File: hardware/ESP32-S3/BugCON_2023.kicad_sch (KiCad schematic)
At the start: 30 parts, among them J1 Conn_01x04_Pin, J2 Conn_01x04_Pin, J3 Conn_01x02, P1 USB_C_Plug_USB2.0, Q1 DMG3415U-7, SW1 RESET, SW2 GPIO, SW3 ON, U1 ESP32-S3-WROOM-1U-N16, U2 AP2112K-3.3

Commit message: Change Place_OLED
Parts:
- C6, C7, C8, C9: provedor (none) -> LCSC
- D1: manf# MBR120LSF -> (none)
- D2, D6, D7, D8: footprint FootprintsB:WS2812B_WDS -> FootprintsB:LED_SK6812MINI_PLCC4_3.5x3.5mm_P1.75mm
- J1: provedor (none) -> Unitelectronic
- J3: footprint Connector_PinSocket_2.54mm:PinSocket_1x02_P2.54mm_Vertical -> FootprintsB:BAT_12BH331P-GR; manf# (none) -> 12BH331P-GR
- P1: LCSC# C2760486 -> C2765186; manf# TYPE-C-31-M-31 -> (none)
- Q1: manf# DMG3415U-7 -> (none)
- R1: LCSC# C217281 -> C309083; manf# CR-03JL7---10K -> (none)
- R2, R3: LCSC# C191782 -> C204548; manf# ERJ3RBD5101V -> (none)
- R4: manf# WR06X104JTL -> (none)
- U2: LCSC# C150742 -> C51118; manf# AP7365-33WG-7 -> (none)
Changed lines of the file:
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@@
+      (effects (font (size 1.27 1.27)) hide)
+    )
+    (property "provedor" "Unitelectronic" (at 24.384 116.967 0)
       (effects (font (size 1.27 1.27)) hide)
     )
@@
       (effects (font (size 1.27 1.27)) hide)
     )
-    (property "manf#" "DMG3415U-7" (at 88.138 27.051 0)
+    (property "manf#" "" (at 88.138 27.051 0)
       (effects (font (size 1.27 1.27)) hide)
     )
@@
       (effects (font (size 1.27 1.27)) hide)
     )
+    (property "provedor" "LCSC" (at 193.294 123.444 0)
+      (effects (font (size 1.27 1.27)) hide)
+    )
     (pin "1")
     (pin "2")
@@
       (effects (font (size 1.27 1.27)))
     )
-    (property "Footprint" "FootprintsB:WS2812B_WDS" (at 236.22 143.129 0)
+    (property "Footprint" "FootprintsB:LED_SK6812MINI_PLCC4_3.5x3.5mm_P1.75mm" (at 236.22 143.129 0)
       (effects (font (size 1.27 1.27)) (justify left top) hide)
     )
@@
       (effects (font (size 1.27 1.27)) hide)
     )
-    (property "manf#" "CR-03JL7---10K" (at 103.124 107.95 0)
-      (effects (font (size 1.27 1.27)) hide)
-    )
-    (property "LCSC#" "C217281" (at 103.124 107.95 0)
+    (property "manf#" "" (at 103.124 107.95 0)
+      (effects (font (size 1.27 1.27)) hide)
+    )
+    (property "LCSC#" "C309083" (at 103.124 107.95 0)
       (effects (font (size 1.27 1.27)) hide)
     )
@@
       (effects (font (size 1.27 1.27)))
     )
-    (property "Footprint" "FootprintsB:WS2812B_WDS" (at 186.563 143.129 0)
+    (property "Footprint" "FootprintsB:LED_SK6812MINI_PLCC4_3.5x3.5mm_P1.75mm" (at 186.563 143.129 0)
       (effects (font (size 1.27 1.27)) (justify left top) hide)
     )
@@
       (effects (font (size 1.27 1.27)) hide)
     )
+    (property "provedor" "LCSC" (at 266.7 123.444 0)
+      (effects (font (size 1.27 1.27)) hide)
+    )
     (pin "1")
     (pin "2")
@@
       (effects (font (size 1.27 1.27)) hide)
     )
+    (property "provedor" "LCSC" (at 242.697 123.444 0)
+      (effects (font (size 1.27 1.27)) hide)
+    )
     (pin "1")
     (pin "2")
@@
       (effects (font (size 1.27 1.27)) hide)
     )
-    (property "manf#" "ERJ3RBD5101V" (at 46.482 26.416 0)
-      (effects (font (size 1.27 1.27)) hide)
-    )
-    (property "LCSC#" "C191782" (at 46.482 26.416 0)
+    (property "manf#" "" (at 46.482 26.416 0)
+      (effects (font (size 1.27 1.27)) hide)
+    )
+    (property "LCSC#" "C204548" (at 46.482 26.416 0)
       (effects (font (size 1.27 1.27)) hide)
     )
@@
       (effects (font (size 1.27 1.27)) hide)
     )
-    (property "manf#" "AP7365-33WG-7" (at 121.158 35.941 0)
+    (property "manf#" "" (at 121.158 35.941 0)
       (effects (font (size 1.27 1.27)) hide)
     )
@@
       (effects (font (size 1.27 1.27)) hide)
     )
-    (property "LCSC#" "C150742" (at 121.158 35.941 0)
+    (property "LCSC#" "C51118" (at 121.158 35.941 0)
       (effects (font (size 1.27 1.27)) hide)
     )
@@
     )
     (property "LCSC#" "C42998" (at 218.186 123.444 0)
+      (effects (font (size 1.27 1.27)) hide)
+    )
+    (property "provedor" "LCSC" (at 218.186 123.444 0)
       (effects (font (size 1.27 1.27)) hide)
     )
@@
       (effects (font (size 1.27 1.27)) (justify left))
     )
-    (property "Footprint" "Connector_PinSocket_2.54mm:PinSocket_1x02_P2.54mm_Vertical" (at 38.1 85.598 0)
+    (property "Footprint" "FootprintsB:BAT_12BH331P-GR" (at 38.1 85.598 0)
       (effects (font (size 1.27 1.27)) hide)
     )
     (property "Datasheet" "~" (at 38.1 85.598 0)
+      (effects (font (size 1.27 1.27)) hide)
+    )
+    (property "manf#" "12BH331P-GR" (at 38.1 85.598 0)
       (effects (font (size 1.27 1.27)) hide)
     )
@@
       (effects (font (size 1.27 1.27)))
     )
-    (property "Footprint" "FootprintsB:WS2812B_WDS" (at 211.836 143.129 0)
+    (property "Footprint" "FootprintsB:LED_SK6812MINI_PLCC4_3.5x3.5mm_P1.75mm" (at 211.836 143.129 0)
       (effects (font (size 1.27 1.27)) (justify left top) hide)
     )
@@
       (effects (font (size 1.27 1.27)) hide)
     )
-    (property "manf#" "ERJ3RBD5101V" (at 46.482 28.956 0)
-      (effects (font (size 1.27 1.27)) hide)
-    )
-    (property "LCSC#" "C191782" (at 46.482 28.956 0)
+    (property "manf#" "" (at 46.482 28.956 0)
+      (effects (font (size 1.27 1.27)) hide)
+    )
+    (property "LCSC#" "C204548" (at 46.482 28.956 0)
       (effects (font (size 1.27 1.27)) hide)
     )
@@
       (effects (font (size 1.27 1.27)) hide)
     )
-    (property "manf#" "TYPE-C-31-M-31" (at 26.924 36.576 0)
-      (effects (font (size 1.27 1.27)) hide)
-    )
-    (property "LCSC#" "C2760486" (at 26.924 36.576 0)
+    (property "manf#" "" (at 26.924 36.576 0)
+      (effects (font (size 1.27 1.27)) hide)
+    )
+    (property "LCSC#" "C2765186" (at 26.924 36.576 0)
       (effects (font (size 1.27 1.27)) hide)
     )
@@
       (effects (font (size 1.27 1.27)))
     )
-    (property "Footprint" "FootprintsB:WS2812B_WDS" (at 260.223 143.129 0)
+    (property "Footprint" "FootprintsB:LED_SK6812MINI_PLCC4_3.5x3.5mm_P1.75mm" (at 260.223 143.129 0)
       (effects (font (size 1.27 1.27)) (justify left top) hide)
     )
@@
       (effects (font (size 1.27 1.27)) hide)
     )
-    (property "manf#" "WR06X104JTL" (at 77.47 40.132 0)
+    (property "manf#" "" (at 77.47 40.132 0)
       (effects (font (size 1.27 1.27)) hide)
     )
@@
       (effects (font (size 1.27 1.27)) hide)
     )
-    (property "manf#" "MBR120LSF" (at 84.455 33.401 0)
-      (effects (font (size 1.27 1.27)) hide)
-    )
+    (property "manf#" "" (at 84.455 33.401 0)
+      (effects (font (size 1.27 1.27)) hide)
+    )

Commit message: Add_Hole
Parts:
- U1: value ESP32-S3-WROOM-1U-N16 -> ESP32-S3-WROOM-1-N4
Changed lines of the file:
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@@
   (symbol (lib_id "ESP32-S3-WROOM:ESP32-S3-WROOM-1-N8") (at 177.419 51.435 0) (unit 1)
     (in_bom yes) (on_board yes) (dnp no) (fields_autoplaced)
-    (property "Reference" "U1" (at 177.292 17.018 0)
+    (property "Reference" "U1" (at 176.657 17.78 0)
       (effects (font (size 1.524 1.524)))
     )
-    (property "Value" "ESP32-S3-WROOM-1U-N16" (at 176.657 19.812 0)
+    (property "Value" "ESP32-S3-WROOM-1-N4" (at 176.657 20.32 0)
       (effects (font (size 1.524 1.524)))
     )

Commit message: Update_PCB
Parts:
- added J4, J5: Conn_01x01_Pin, Connector_PinHeader_1.00mm:PinHeader_1x01_P1.00mm_Horizontal, symbol Connector:Conn_01x01_Pin
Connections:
- net TCH2: now reaches U1.11 (IO18)
- net TCH2: now also J4.1 (Pin_1)
- net TCH1: now reaches U1.7 (IO7)
- net TCH1: now also J5.1 (Pin_1)
- no-connect marks 29 -> 27
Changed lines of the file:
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@@
   (no_connect (at 156.337 68.072))
   (no_connect (at 196.977 68.072))
-  (no_connect (at 156.337 52.832))
   (no_connect (at 196.977 60.452))
   (no_connect (at 156.337 45.212))
   (no_connect (at 156.337 50.292))
   (no_connect (at 196.977 75.692))
-  (no_connect (at 156.337 42.672))
   (no_connect (at 196.977 55.372))
   (no_connect (at 196.977 73.152))
@@
     (stroke (width 0) (type default))
   )
+  (wire (pts (xy 250.063 41.91) (xy 254.762 41.91))
+    (stroke (width 0) (type default))
+  )
   (wire (pts (xy 109.728 35.941) (xy 113.538 35.941))
     (stroke (width 0) (type default))
@@
     (stroke (width 0) (type default))
   )
+  (wire (pts (xy 154.305 42.672) (xy 156.337 42.672))
+    (stroke (width 0) (type default))
+  )
+  (wire (pts (xy 154.051 52.832) (xy 156.337 52.832))
+    (stroke (width 0) (type default))
+  )
   (wire (pts (xy 106.426 40.513) (xy 106.426 41.529))
     (stroke (width 0) (type default))
@@
   )
   (wire (pts (xy 51.562 26.416) (xy 51.562 28.956))
+    (stroke (width 0) (type default))
+  )
+  (wire (pts (xy 250.063 35.433) (xy 254.762 35.433))
     (stroke (width 0) (type default))
   )
@@
     (effects (font (size 1.27 1.27)) (justify left bottom))
   )
+  (label "TCH1" (at 250.063 41.91 180) (fields_autoplaced)
+    (effects (font (size 1.27 1.27)) (justify right bottom))
+  )
   (label "TX" (at 199.263 37.592 0) (fields_autoplaced)
     (effects (font (size 1.27 1.27)) (justify left bottom))
@@
     (effects (font (size 1.27 1.27)) (justify left bottom))
   )
+  (label "TCH1" (at 154.305 42.672 180) (fields_autoplaced)
+    (effects (font (size 1.27 1.27)) (justify right bottom))
+  )
   (label "SDA" (at 154.305 62.992 180) (fields_autoplaced)
     (effects (font (size 1.27 1.27)) (justify right bottom))
   )
+  (label "TCH2" (at 154.051 52.832 180) (fields_autoplaced)
+    (effects (font (size 1.27 1.27)) (justify right bottom))
+  )
   (label "RST" (at 150.622 32.512 0) (fields_autoplaced)
     (effects (font (size 1.27 1.27)) (justify left bottom))
@@
   (label "D-" (at 154.305 57.912 0) (fields_autoplaced)
     (effects (font (size 1.27 1.27)) (justify left bottom))
+  )
+  (label "TCH2" (at 250.063 35.433 180) (fields_autoplaced)
+    (effects (font (size 1.27 1.27)) (justify right bottom))
   )
   (label "RST" (at 105.2576 111.506 0) (fields_autoplaced)
@@
     )
   )
+  (symbol (lib_id "Connector:Conn_01x01_Pin") (at 259.842 41.91 180) (unit 1)
+    (in_bom yes) (on_board yes) (dnp no) (fields_autoplaced)
+    (property "Reference" "J5" (at 259.207 36.957 0)
+      (effects (font (size 1.27 1.27)))
+    )
+    (property "Value" "Conn_01x01_Pin" (at 259.207 39.497 0)
+      (effects (font (size 1.27 1.27)))
+    )
+    (property "Footprint" "Connector_PinHeader_1.00mm:PinHeader_1x01_P1.00mm_Horizontal" (at 259.842 41.91 0)
+      (effects (font (size 1.27 1.27)) hide)
+    )
+    (property "Datasheet" "~" (at 259.842 41.91 0)
+      (effects (font (size 1.27 1.27)) hide)
+    )
+    (pin "1")
+    (instances
+      (project "BugCON_2023"
+        (path "/3bd1d1f8-54bc-46fd-8763-4ee40cf8320e"
+          (reference "J5") (unit 1)
+        )
+      )
+    )
+  )
   (symbol (lib_id "Connector:Conn_01x04_Pin") (at 24.384 116.967 0) (unit 1)
     (in_bom yes) (on_board yes) (dnp no) (fields_autoplaced)
@@
         )
       )
+    )
+  )
+  (symbol (lib_id "Connector:Conn_01x01_Pin") (at 259.842 35.433 180) (unit 1)
+    (in_bom yes) (on_board yes) (dnp no) (fields_autoplaced)
+    (property "Reference" "J4" (at 259.207 30.48 0)
+      (effects (font (size 1.27 1.27)))
+    )
+    (property "Value" "Conn_01x01_Pin" (at 259.207 33.02 0)
+      (effects (font (size 1.27 1.27)))
+    )
+    (property "Footprint" "Connector_PinHeader_1.00mm:PinHeader_1x01_P1.00mm_Horizontal" (at 259.842 35.433 0)
+      (effects (font (size 1.27 1.27)) hide)
+    )
+    (property "Datasheet" "~" (at 259.842 35.433 0)
+      (effects (font (size 1.27 1.27)) hide)
+    )
+    (pin "1")
+    (instances
+      (project "BugCON_2023"
+        (path "/3bd1d1f8-54bc-46fd-8763-4ee40cf8320e"
+          (reference "J4") (unit 1)
+        )
+      )

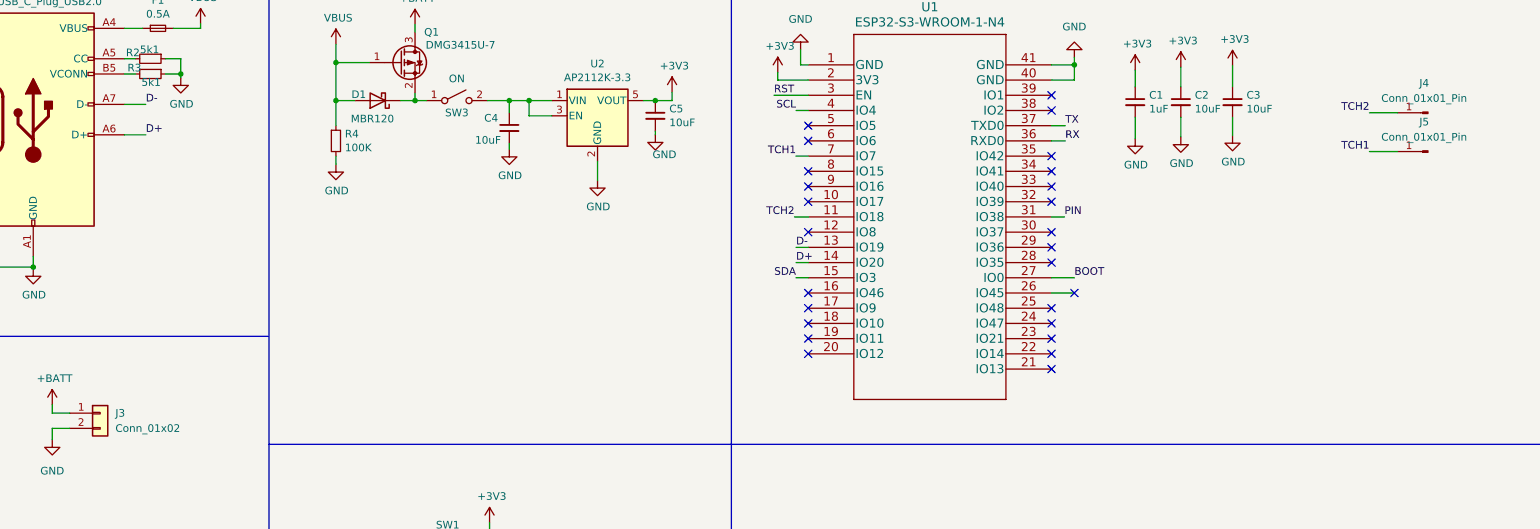
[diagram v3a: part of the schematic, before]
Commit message: upd BOM on esp32 badge
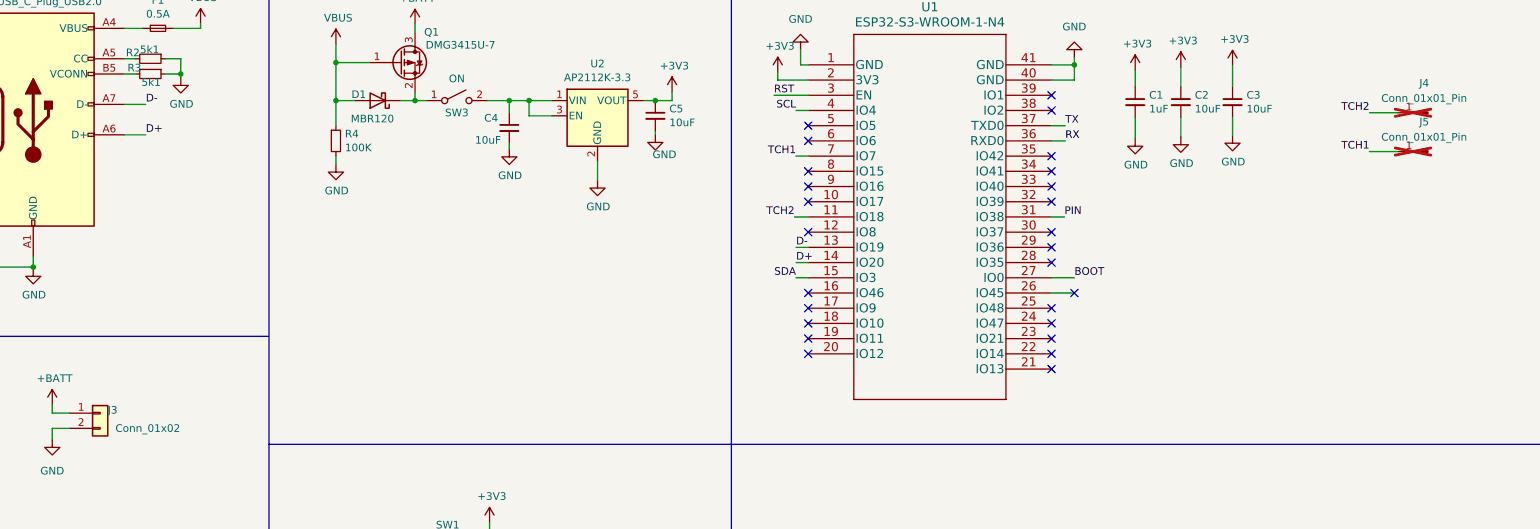
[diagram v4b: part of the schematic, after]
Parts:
- C1: Proveedor (none) -> LCSC; manf# (none) -> CL10A105KB8NNNC; provedor LCSC -> (none)
- C2, C3, C4, C5: Proveedor (none) -> LCSC; manf# (none) -> CL10A106MP8NNNC; provedor LCSC -> (none)
- C6, C7, C8, C9: Proveedor (none) -> LCSC; manf# (none) -> 0603F104M500NT; provedor LCSC -> (none)
- D1: Proveedor (none) -> LCSC; manf# (none) -> MBR120LSF; provedor LCSC -> (none)
- D2, D6, D7, D8: Proveedor (none) -> LCSC; manf# (none) -> WS2812B-Mini
- F1, U1: Proveedor (none) -> MOUSER; provedor MOUSER -> (none)
- J1: Proveedor (none) -> Unit Electronics; provedor Unitelectronic -> (none)
- J2: Proveedor (none) -> -- mixed values --
- J3: Proveedor (none) -> MOUSER
- J4, J5: now not fitted
- P1: Proveedor (none) -> LCSC; manf# (none) -> TYPE-C 16PIN 2MD(073); provedor LCSC -> (none)
- Q1: Proveedor (none) -> LCSC; manf# (none) -> DMG3415U-7; provedor LCSC -> (none)
- R1: Proveedor (none) -> LCSC; manf# (none) -> ARG03BTC1002; provedor LCSC -> (none)
- R2, R3: LCSC# C204548 -> C191782; Proveedor (none) -> LCSC; manf# (none) -> ERJ3RBD5101V; provedor LCSC -> (none)
- R4: Proveedor (none) -> LCSC; manf# (none) -> 0603WAJ0104T5E; provedor LCSC -> (none)
- R9: manf# (none) -> RTT03471JTP
- SW1, SW2: Proveedor (none) -> LCSC; manf# (none) -> TS-1187A-C-C-B; provedor LCSC -> (none)
- SW3: Proveedor (none) -> LCSC; manf# (none) -> SK12D07VG4; provedor LCSC -> (none)
- U2: Proveedor (none) -> LCSC; manf# (none) -> AP2112K-3.3TRG1; provedor LCSC -> (none)
